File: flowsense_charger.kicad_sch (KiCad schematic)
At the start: 34 parts, among them J1 SOLAR, J2 LOAD, J3 Conn_01x02_Pin, J4 LOAD, J5 USB_A, J6 Conn_01x02_Pin, J7 SOLAR, SW1 SW_Push, U1 BQ25185, U2 TPS61230DRC

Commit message: Starts implementing non-regulated output, and alternative 3.3v regulated output.
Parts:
- added J8: Conn_01x02_Pin, Connector_JST:JST_PH_B2B-PH-K_1x02_P2.00mm_Vertical, symbol Connector:Conn_01x02_Pin
- added J9: Conn_01x02_Pin, TerminalBlock_Phoenix:TerminalBlock_Phoenix_MPT-0,5-2-2.54_1x02_P2.54mm_Horizontal, symbol Connector:Conn_01x02_Pin
- added JP2: Jumper_3_Bridged12, Connector_PinHeader_2.54mm:PinHeader_1x03_P2.54mm_Vertical, symbol Jumper:Jumper_3_Bridged12
- added R4: 230K, Resistor_SMD:R_1206_3216Metric, symbol Device:R
- added U3: BQ24074RGT, Package_DFN_QFN:VQFN-16-1EP_3x3mm_P0.5mm_EP1.6x1.6mm, symbol Battery_Management:BQ24074RGT
- C6: footprint (none) -> Capacitor_SMD:C_0805_2012Metric
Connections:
- net +5V: no longer C5.1, J2.2 (Pin_2), J4.2 (Pin_2), J5.1 (VBUS), R5.2, R6.1, U2.3 (VOUT), U2.4 (VOUT)
- net GND: now also C5.1, J8.2 (Pin_2), J9.2 (Pin_2); no longer C5.2
- net V_SYS: now also J8.1 (Pin_1), J9.1 (Pin_1)
- net SET_V: now reaches R7.1, U2.7 (FB)
- net SET_V: now also JP2.2 (C); no longer R6.2
- new net: JP2.1 (A), R6.2
- new net: JP2.3 (B), R4.1
- new net: U3.10 (OUT), U3.11 (OUT)
- new net: U3.17 (VSS), U3.8 (VSS)
- new net: U3.2 (BAT), U3.3 (BAT)
- new net VCC: C5.2, J2.2 (Pin_2), J4.2 (Pin_2), R4.2, R5.2, R6.1, U2.3 (VOUT), U2.4 (VOUT)
- new net VOUT: J5.1 (VBUS)
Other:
- note added: "Setting voltage from to either 5v or to 3.3v"
- note added: "TODO intergrate BQ24D74 or LTC4000 or BQ25798"
- note removed: "Switching Voltage regulator (not linear because this is for a battery powered device!)"
- moved on the sheet: C5, JP2_500mA_4.2v1, R2, R5, R6, R7, TP1, TP2, TP3

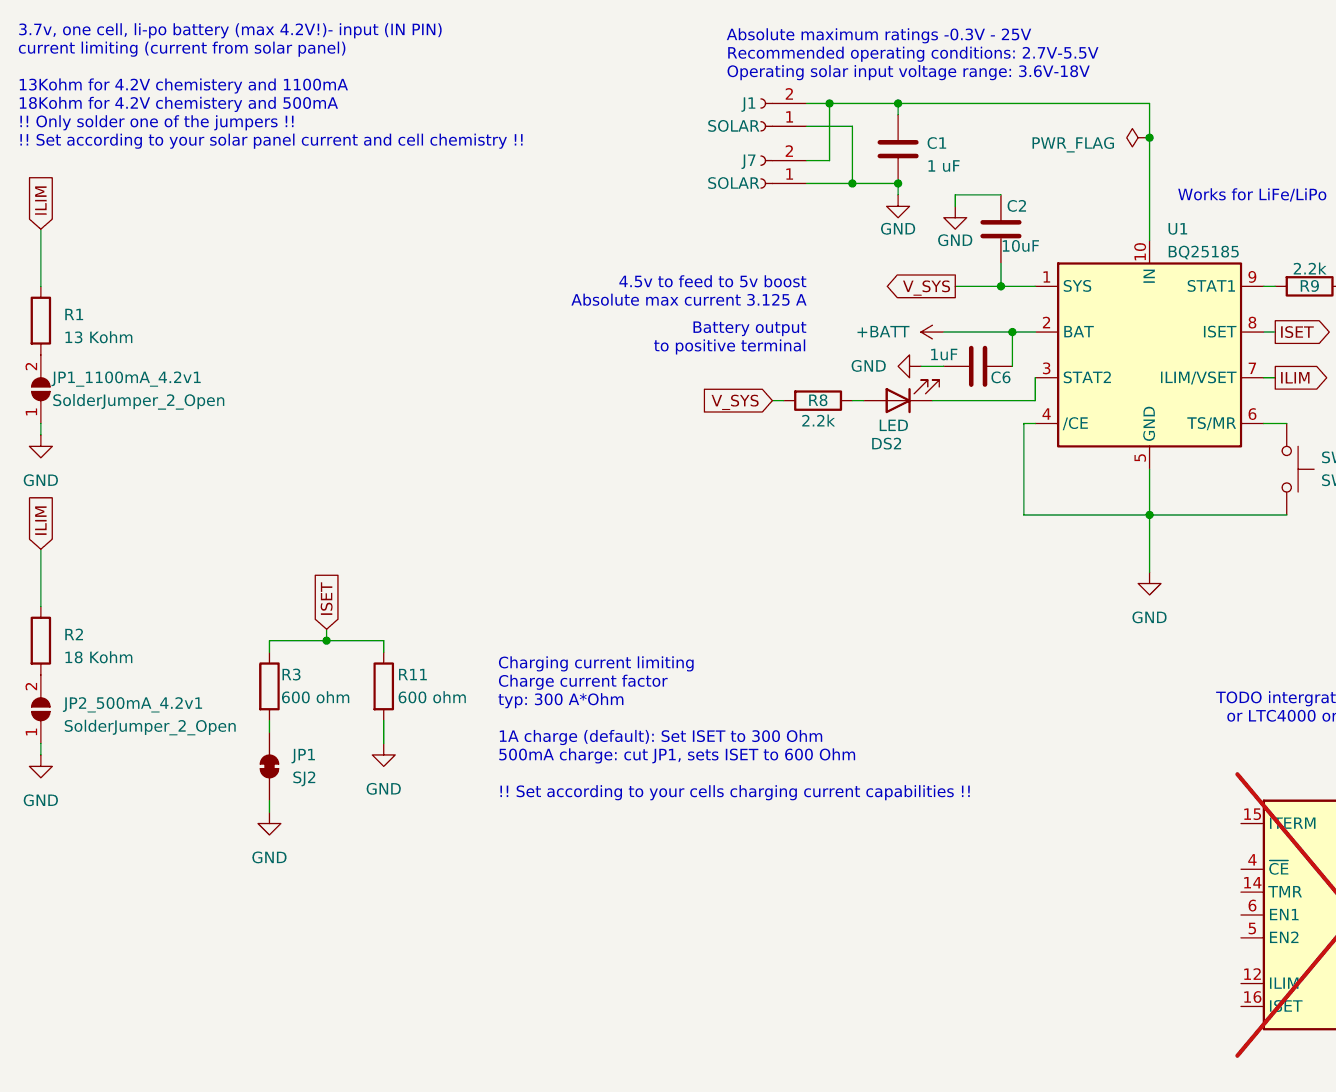
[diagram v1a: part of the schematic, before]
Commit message: Rearrange text on schematic a bit
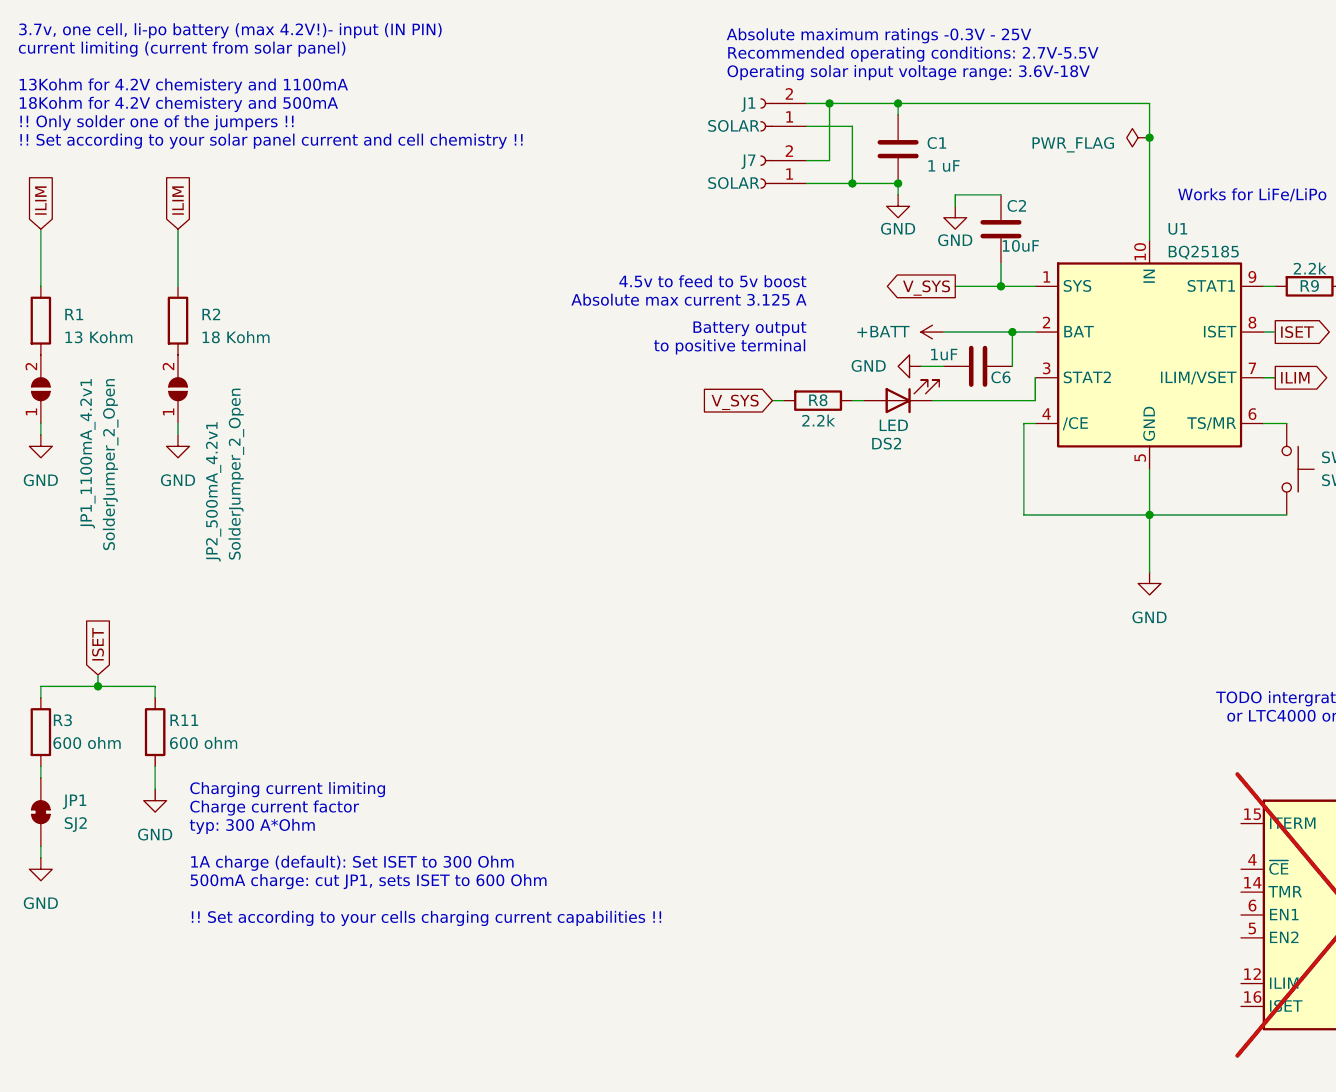
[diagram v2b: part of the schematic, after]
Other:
- moved on the sheet: JP1, JP2_500mA_4.2v1, R11, R2, R3
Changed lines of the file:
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@@
 	(text "Charging current limiting\nCharge current factor \ntyp: 300 A*Ohm\n\n1A charge (default): Set ISET to 300 Ohm\n500mA charge: cut JP1, sets ISET to 600 Ohm\n\n!! Set according to your cells charging current capabilities !!"
 		(exclude_from_sim no)
-		(at 66.04 99.06 0)
+		(at 31.75 113.03 0)
 		(effects
 			(font
@@
 	)
 	(junction
-		(at 46.99 81.28)
+		(at 21.59 86.36)
 		(diameter 0)
 		(color 0 0 0 0)
@@
 	(wire
 		(pts
-			(xy 46.99 80.01) (xy 46.99 81.28)
+			(xy 21.59 85.09) (xy 21.59 86.36)
 		)
 		(stroke
@@
 	(wire
 		(pts
-			(xy 40.64 81.28) (xy 46.99 81.28)
+			(xy 15.24 86.36) (xy 21.59 86.36)
 		)
 		(stroke
@@
 	(wire
 		(pts
-			(xy 40.64 81.28) (xy 40.64 82.55)
+			(xy 15.24 86.36) (xy 15.24 87.63)
 		)
 		(stroke
@@
 	(wire
 		(pts
-			(xy 15.24 71.12) (xy 15.24 77.47)
+			(xy 30.48 35.56) (xy 30.48 41.91)
 		)
 		(stroke
@@
 	(wire
 		(pts
-			(xy 53.34 81.28) (xy 53.34 82.55)
+			(xy 27.94 86.36) (xy 27.94 87.63)
 		)
 		(stroke
@@
 	(wire
 		(pts
-			(xy 15.24 92.71) (xy 15.24 93.98)
+			(xy 30.48 57.15) (xy 30.48 58.42)
 		)
 		(stroke
@@
 	(wire
 		(pts
-			(xy 40.64 99.06) (xy 40.64 100.33)
+			(xy 15.24 104.14) (xy 15.24 105.41)
 		)
 		(stroke
@@
 	(wire
 		(pts
-			(xy 53.34 90.17) (xy 53.34 92.71)
+			(xy 27.94 95.25) (xy 27.94 97.79)
 		)
 		(stroke
@@
 	(wire
 		(pts
-			(xy 46.99 81.28) (xy 53.34 81.28)
+			(xy 21.59 86.36) (xy 27.94 86.36)
 		)
 		(stroke
@@
 	(wire
 		(pts
-			(xy 40.64 91.44) (xy 40.64 90.17)
+			(xy 15.24 96.52) (xy 15.24 95.25)
 		)
 		(stroke
@@
 	(global_label "ISET"
 		(shape input)
-		(at 46.99 80.01 90)
+		(at 21.59 85.09 90)
 		(fields_autoplaced yes)
 		(effects
@@
 		)
 		(property "Intersheetrefs" "${INTERSHEET_REFS}"
-			(at 46.99 73.0939 90)
+			(at 21.59 78.1739 90)
 			(effects
 				(font
@@
 	(global_label "ILIM"
 		(shape input)
-		(at 15.24 71.12 90)
+		(at 30.48 35.56 90)
 		(fields_autoplaced yes)
 		(effects
@@
 		)
 		(property "Intersheetrefs" "${INTERSHEET_REFS}"
-			(at 15.24 64.5251 90)
+			(at 30.48 28.9651 90)
 			(effects
 				(font
@@
 	(symbol
 		(lib_id "Device:R")
-		(at 53.34 86.36 0)
+		(at 27.94 91.44 0)
 		(unit 1)
 		(exclude_from_sim no)
@@
 		(dnp no)
 		(property "Reference" "R11"
-			(at 54.864 85.09 0)
+			(at 29.464 90.17 0)
 			(effects
 				(font
@@
 		)
 		(property "Value" "600 ohm"
-			(at 54.864 87.63 0)
+			(at 29.464 92.71 0)
 			(effects
 				(font
@@
 		)
 		(property "Footprint" "Resistor_SMD:R_1206_3216Metric"
-			(at 51.562 86.36 90)
+			(at 26.162 91.44 90)
 			(effects
 				(font
@@
 		)
 		(property "Datasheet" "~"
-			(at 53.34 86.36 0)
+			(at 27.94 91.44 0)
 			(effects
 				(font
@@
 		)
 		(property "Description" ""
-			(at 53.34 86.36 0)
+			(at 27.94 91.44 0)
 			(effects
 				(font
@@
 	(symbol
 		(lib_id "Jumper:SolderJumper_2_Bridged")
-		(at 40.64 95.25 90)
+		(at 15.24 100.33 90)
 		(unit 1)
 		(exclude_from_sim no)
@@
 		(fields_autoplaced yes)
 		(property "Reference" "JP1"
-			(at 43.18 93.9799 90)
+			(at 17.78 99.0599 90)
 			(effects
 				(font
@@
 		)
 		(property "Value" "SJ2"
-			(at 43.18 96.5199 90)
+			(at 17.78 101.5999 90)
 			(effects
 				(font
@@
 		)
 		(property "Footprint" "Jumper:SolderJumper-2_P1.3mm_Bridged_Pad1.0x1.5mm"
-			(at 40.64 95.25 0)
+			(at 15.24 100.33 0)
 			(effects
 				(font
@@
 		)
 		(property "Datasheet" "~"
-			(at 40.64 95.25 0)
+			(at 15.24 100.33 0)
 			(effects
 				(font
@@
 		)
 		(property "Description" "Solder Jumper, 2-pole, closed/bridged"
-			(at 40.64 95.25 0)
+			(at 15.24 100.33 0)
 			(effects
 				(font
@@
 	(symbol
 		(lib_id "Device:R")
-		(at 40.64 86.36 0)
+		(at 15.24 91.44 0)
 		(unit 1)
 		(exclude_from_sim no)
@@
 		(dnp no)
 		(property "Reference" "R3"
-			(at 41.91 85.09 0)
+			(at 16.51 90.17 0)
 			(effects
 				(font
@@
 		)
 		(property "Value" "600 ohm"
-			(at 41.91 87.63 0)
+			(at 16.51 92.71 0)
 			(effects
 				(font
@@
 		)
 		(property "Footprint" "Resistor_SMD:R_1206_3216Metric"
-			(at 38.862 86.36 90)
+			(at 13.462 91.44 90)
 			(effects
 				(font
@@
 		)
 		(property "Datasheet" "~"
-			(at 40.64 86.36 0)
+			(at 15.24 91.44 0)
 			(effects
 				(font
@@
 		)
 		(property "Description" ""
-			(at 40.64 86.36 0)
+			(at 15.24 91.44 0)
 			(effects
 				(font
@@
 		(lib_name "GND_3")
 		(lib_id "power:GND")
-		(at 15.24 93.98 0)
+		(at 30.48 58.42 0)
 		(unit 1)
 		(exclude_from_sim no)
@@
 		(fields_autoplaced yes)
 		(property "Reference" "#PWR031"
-			(at 15.24 100.33 0)
+			(at 30.48 64.77 0)
 			(effects
 				(font
@@
 		)
 		(property "Value" "GND"
-			(at 15.24 99.06 0)
+			(at 30.48 63.5 0)
 			(effects
 				(font
@@
 		)
 		(property "Footprint" ""
-			(at 15.24 93.98 0)
+			(at 30.48 58.42 0)
 			(effects
 				(font
@@
 		)
 		(property "Datasheet" ""
-			(at 15.24 93.98 0)
+			(at 30.48 58.42 0)
 			(effects
 				(font
@@
 		)
 		(property "Description" "Power symbol creates a global label with name \"GND\" , ground"
-			(at 15.24 93.98 0)
+			(at 30.48 58.42 0)
 			(effects
 				(font
@@
 		(lib_name "GND_6")
 		(lib_id "power:GND")
-		(at 40.64 100.33 0)
+		(at 15.24 105.41 0)
 		(unit 1)
 		(exclude_from_sim no)
@@
 		(fields_autoplaced yes)
 		(property "Reference" "#PWR015"
-			(at 40.64 106.68 0)
+			(at 15.24 111.76 0)
 			(effects
 				(font
@@
 		)
 		(property "Value" "GND"
-			(at 40.64 105.41 0)
+			(at 15.24 110.49 0)
 			(effects
 				(font
@@
 		)
 		(property "Footprint" ""
-			(at 40.64 100.33 0)
+			(at 15.24 105.41 0)
 			(effects
 				(font
@@
 		)
 		(property "Datasheet" ""
-			(at 40.64 100.33 0)
+			(at 15.24 105.41 0)
 			(effects
 				(font
@@
 		)
 		(property "Description" "Power symbol creates a global label with name \"GND\" , ground"
-			(at 40.64 100.33 0)
+			(at 15.24 105.41 0)
 			(effects
 				(font
@@
 		(dnp no)
 		(property "Reference" "JP1_1100mA_4.2v1"
-			(at 16.51 52.07 90)
+			(at 20.32 52.07 0)
 			(effects
 				(font
@@
 		)
 		(property "Value" "SolderJumper_2_Open"
-			(at 16.51 54.61 90)
+			(at 22.86 52.07 0)
 			(effects
 				(font
@@
 	(symbol
 		(lib_id "Device:R")
-		(at 15.24 81.28 0)
+		(at 30.48 45.72 0)
 		(unit 1)
 		(exclude_from_sim no)
@@
 		(fields_autoplaced yes)
 		(property "Reference" "R2"
-			(at 17.78 80.645 0)
+			(at 33.02 45.085 0)
 			(effects
 				(font
@@
 		)
 		(property "Value" "18 Kohm"
-			(at 17.78 83.185 0)
+			(at 33.02 47.625 0)
 			(effects
 				(font
@@
 		)
 		(property "Footprint" "Resistor_SMD:R_1206_3216Metric"
-			(at 13.462 81.28 90)
+			(at 28.702 45.72 90)
 			(effects
 				(font
@@
 		)
 		(property "Datasheet" "~"
-			(at 15.24 81.28 0)
+			(at 30.48 45.72 0)
 			(effects
 				(font
@@
 		)
 		(property "Description" ""
-			(at 15.24 81.28 0)
+			(at 30.48 45.72 0)
 			(effects
 				(font
@@
 	(symbol
 		(lib_id "Jumper:SolderJumper_2_Open")
-		(at 15.24 88.9 90)
+		(at 30.48 53.34 90)
 		(unit 1)
 		(exclude_from_sim no)
@@
 		(on_board yes)
 		(dnp no)
-		(fields_autoplaced yes)
 		(property "Reference" "JP2_500mA_4.2v1"
-			(at 17.78 88.265 90)
+			(at 34.29 72.39 0)
 			(effects
 				(font
 					(size 1.27 1.27)
 				)
-				(justify right)
+				(justify left)
 			)
 		)
 		(property "Value" "SolderJumper_2_Open"
-			(at 17.78 90.805 90)
+			(at 36.83 72.39 0)
 			(effects
 				(font
 					(size 1.27 1.27)
 				)
-				(justify right)
+				(justify left)
 			)
 		)
 		(property "Footprint" "Jumper:SolderJumper-2_P1.3mm_Open_Pad1.0x1.5mm"
-			(at 15.24 88.9 0)
+			(at 30.48 53.34 0)
 			(effects
 				(font
@@
 		)
 		(property "Datasheet" "~"
-			(at 15.24 88.9 0)
+			(at 30.48 53.34 0)
 			(effects
 				(font
@@
 		)
 		(property "Description" ""
-			(at 15.24 88.9 0)
+			(at 30.48 53.34 0)
 			(effects
 				(font
@@
 		(lib_name "GND_6")
 		(lib_id "power:GND")
-		(at 53.34 92.71 0)
+		(at 27.94 97.79 0)
 		(unit 1)
 		(exclude_from_sim no)
@@
 		(fields_autoplaced yes)
 		(property "Reference" "#PWR02"
-			(at 53.34 99.06 0)
+			(at 27.94 104.14 0)
 			(effects
 				(font
@@
 		)
 		(property "Value" "GND"
-			(at 53.34 97.79 0)
+			(at 27.94 102.87 0)
 			(effects
 				(font
@@
 		)
 		(property "Footprint" ""
-			(at 53.34 92.71 0)
+			(at 27.94 97.79 0)
 			(effects
 				(font
@@
 		)
 		(property "Datasheet" ""
-			(at 53.34 92.71 0)
+			(at 27.94 97.79 0)
 			(effects
 				(font
@@
 		)
 		(property "Description" "Power symbol creates a global label with name \"GND\" , ground"
-			(at 53.34 92.71 0)
+			(at 27.94 97.79 0)
 			(effects
 				(font

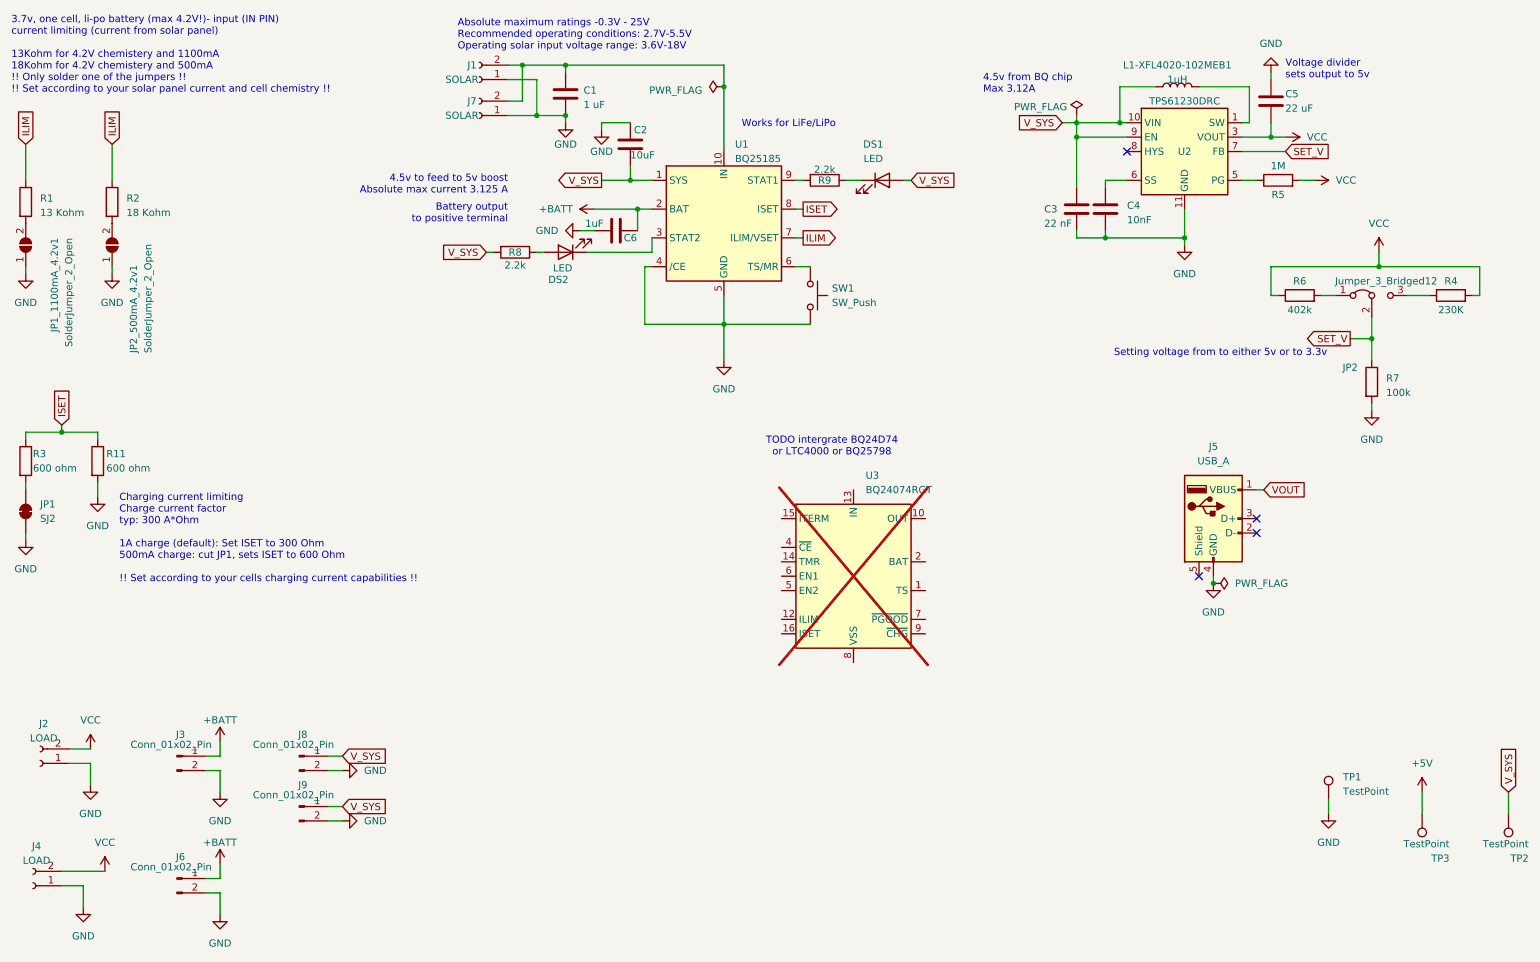
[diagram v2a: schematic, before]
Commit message: Layout all components on a single face for easier manufacturing
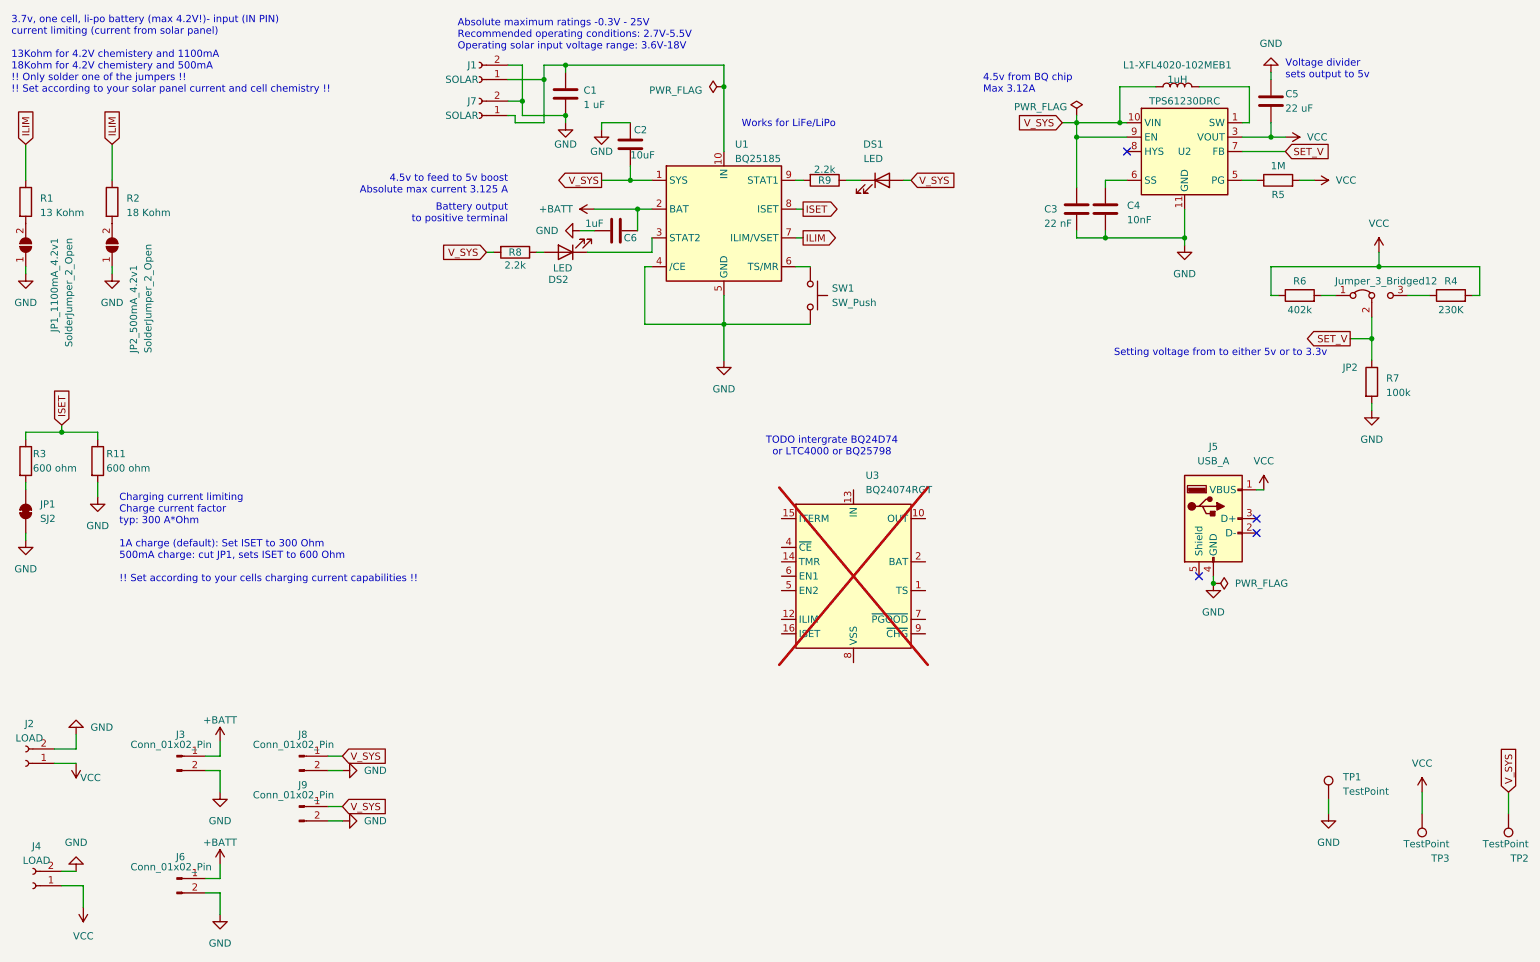
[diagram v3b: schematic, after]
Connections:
- net +5V is gone; now on net VCC: TP3.1
- net VOUT is gone; now on net VCC: J5.1 (VBUS)
- net GND: now also J1.2 (Pin_2), J2.2 (Pin_2), J4.2 (Pin_2), J7.2 (Pin_2); no longer J1.1 (Pin_1), J2.1 (Pin_1), J4.1 (Pin_1), J7.1 (Pin_1)
- net VCC: now also J2.1 (Pin_1), J4.1 (Pin_1); no longer J2.2 (Pin_2), J4.2 (Pin_2)
- net at C1.1, U1.10 (IN): now also J1.1 (Pin_1), J7.1 (Pin_1); no longer J1.2 (Pin_2), J7.2 (Pin_2)
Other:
- moved on the sheet: J2
